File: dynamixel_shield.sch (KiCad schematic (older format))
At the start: 21 parts, among them P1 BARREL_JACK, P2 CONN_01X02, P3 CONN_01X03, P4 CONN_01X03, P5 CONN_01X03, P6 CONN_01X03, P7 CONN_01X03, P8 CONN_01X03, P9 CONN_01X03, Q1 MOSFET_N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

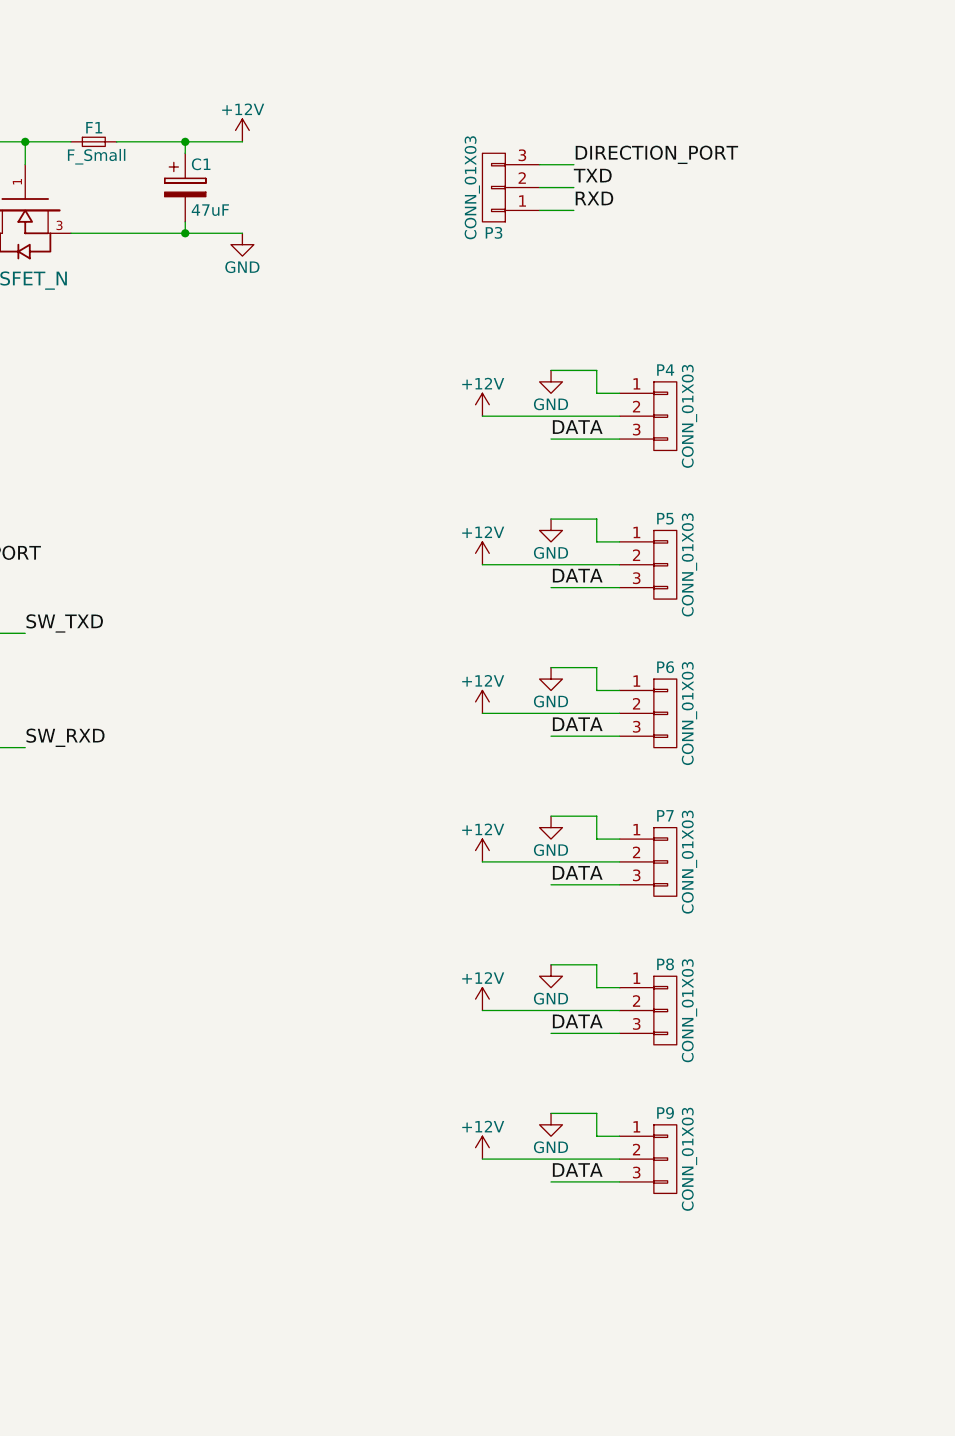
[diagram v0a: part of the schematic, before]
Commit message: Add power on LED
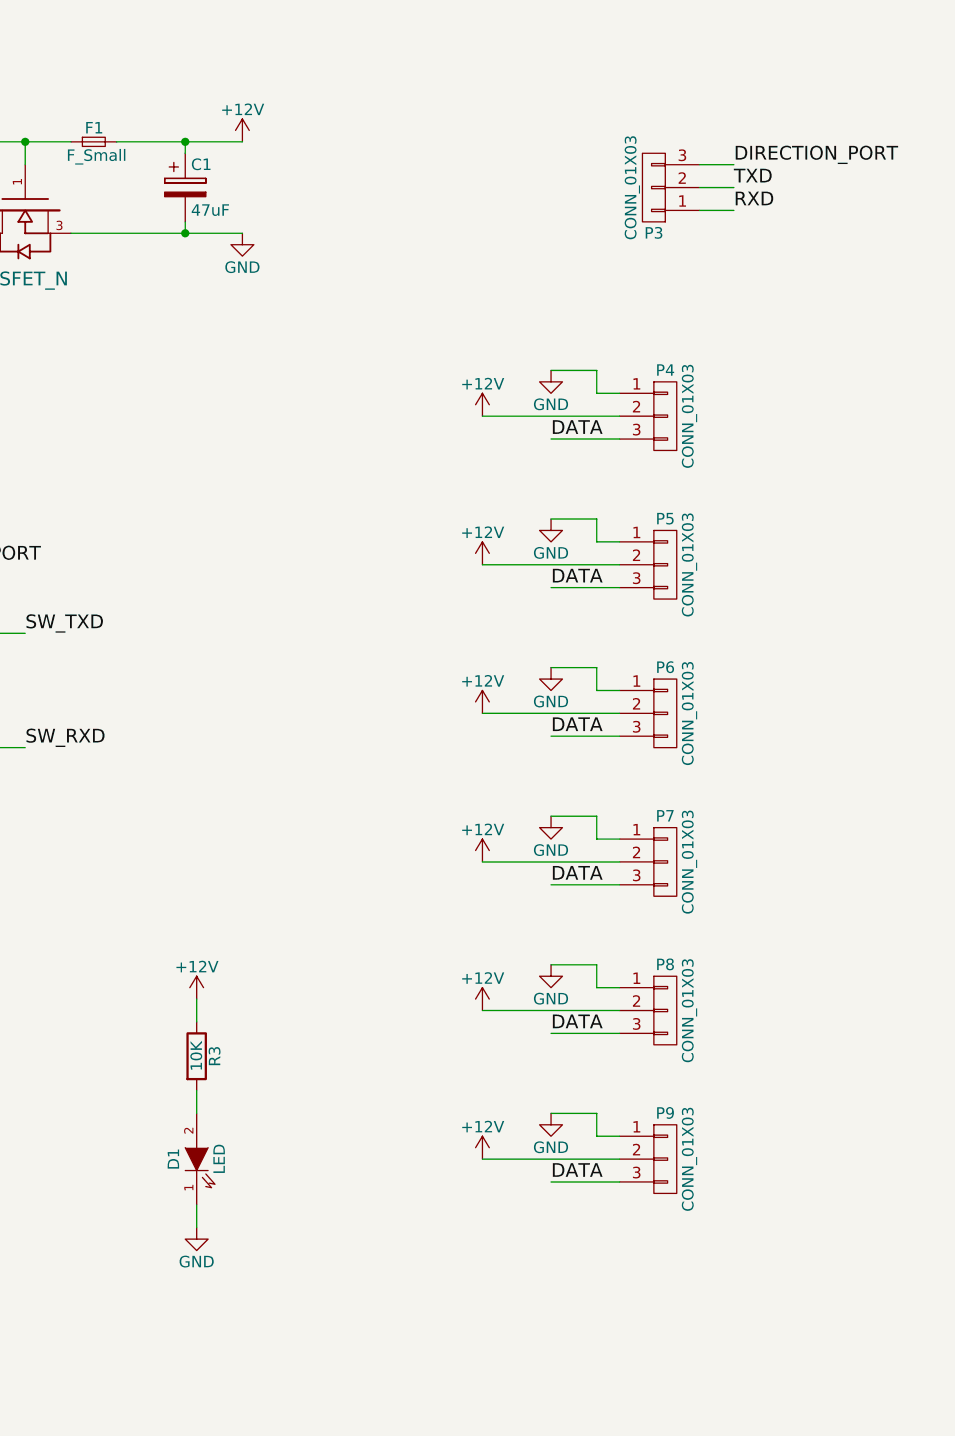
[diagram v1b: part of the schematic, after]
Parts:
- added D1: LED, LEDs:LED_0603, symbol LED
- added R3: 10K, Resistors_SMD:R_0603_HandSoldering, symbol R
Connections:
- net +12V: now also R3.1
- net GND: now also D1.1 (K)
- new net: D1.2 (A), R3.2
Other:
- moved on the sheet: P3
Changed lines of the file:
@@
 Text Label 3600 6650 0    60   ~ 0
 SW_RXD
-Text Label 9100 1550 0    60   ~ 0
+Text Label 9800 1550 0    60   ~ 0
 RXD
-Text Label 9100 1450 0    60   ~ 0
+Text Label 9800 1450 0    60   ~ 0
 TXD
-Text Label 9100 1350 0    60   ~ 0
+Text Label 9800 1350 0    60   ~ 0
 DIRECTION_PORT
 Text Label 6050 3100 0    60   ~ 0
@@
 L CONN_01X03 P3
 U 1 1 57B600E0
-P 8750 1450
-F 0 "P3" H 8750 1650 50  0000 C CNN
-F 1 "CONN_01X03" V 8850 1450 50  0000 C CNN
-F 2 "Pin_Headers:Pin_Header_Angled_1x03" H 8750 1450 50  0001 C CNN
-F 3 "" H 8750 1450 50  0000 C CNN
-	1    8750 1450
+P 9450 1450
+F 0 "P3" H 9450 1650 50  0000 C CNN
+F 1 "CONN_01X03" V 9550 1450 50  0000 C CNN
+F 2 "Pin_Headers:Pin_Header_Angled_1x03" H 9450 1450 50  0001 C CNN
+F 3 "" H 9450 1450 50  0000 C CNN
+	1    9450 1450
 	-1   0    0    1
 $EndComp
@@
 	3400 6650 3600 6650
 Wire Wire Line
-	8950 1350 9100 1350
-Wire Wire Line
-	9100 1450 8950 1450
-Wire Wire Line
-	8950 1550 9100 1550
+	9650 1350 9800 1350
+Wire Wire Line
+	9800 1450 9650 1450
+Wire Wire Line
+	9650 1550 9800 1550
 Wire Wire Line
 	4550 2850 5800 2850
@@
 Wire Wire Line
 	6000 1650 6100 1650
+$Comp
+L LED D1
+U 1 1 57BDD735
+P 7450 5700
+F 0 "D1" H 7450 5800 50  0000 C CNN
+F 1 "LED" H 7450 5600 50  0000 C CNN
+F 2 "LEDs:LED_0603" H 7450 5700 50  0001 C CNN
+F 3 "" H 7450 5700 50  0000 C CNN
+	1    7450 5700
+	0    -1   -1   0
+$EndComp
+$Comp
+L R R3
+U 1 1 57BDD91F
+P 7450 5250
+F 0 "R3" V 7530 5250 50  0000 C CNN
+F 1 "10K" V 7450 5250 50  0000 C CNN
+F 2 "Resistors_SMD:R_0603_HandSoldering" V 7380 5250 50  0001 C CNN
+F 3 "" H 7450 5250 50  0000 C CNN
+	1    7450 5250
+	1    0    0    -1
+$EndComp
+Wire Wire Line
+	7450 5400 7450 5500
+$Comp
+L +12V #PWR?
+U 1 1 57BDE386
+P 7450 5000
+F 0 "#PWR?" H 7450 4850 50  0001 C CNN
+F 1 "+12V" H 7450 5140 50  0000 C CNN
+F 2 "" H 7450 5000 50  0000 C CNN
+F 3 "" H 7450 5000 50  0000 C CNN
+	1    7450 5000
+	1    0    0    -1
+$EndComp
+$Comp
+L GND #PWR?
+U 1 1 57BDE3DF
+P 7450 6000
+F 0 "#PWR?" H 7450 5750 50  0001 C CNN
+F 1 "GND" H 7450 5850 50  0000 C CNN
+F 2 "" H 7450 6000 50  0000 C CNN
+F 3 "" H 7450 6000 50  0000 C CNN
+	1    7450 6000
+	1    0    0    -1
+$EndComp
+Wire Wire Line
+	7450 5000 7450 5100
+Wire Wire Line
+	7450 5900 7450 6000
 $EndSCHEMATC

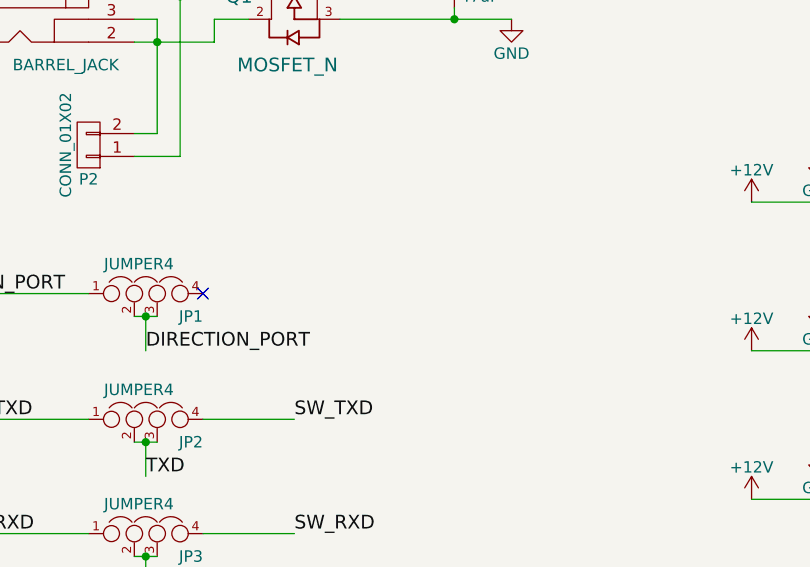
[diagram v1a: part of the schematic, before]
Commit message: Fix error in schematics
Arduino direction port was not connected in the SW configuration.
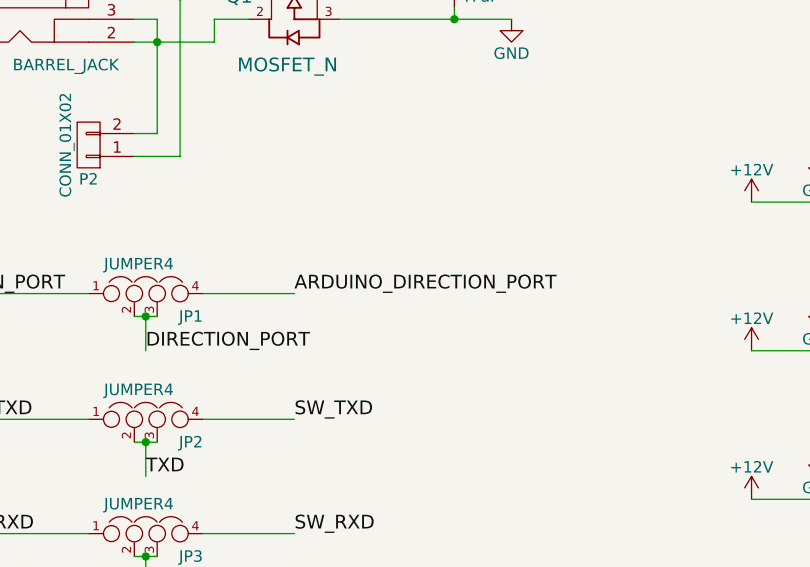
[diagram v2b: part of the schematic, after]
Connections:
- net ARDUINO_DIRECTION_PORT: now also JP1.4
- no-connect marks 26 -> 25
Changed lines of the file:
@@
 	1    0    0    -1
 $EndComp
-NoConn ~ 6300 2850
 Wire Wire Line
 	2100 5600 1900 5600
@@
 Wire Wire Line
 	7450 5900 7450 6000
+Text Label 6700 2850 0    60   ~ 0
+ARDUINO_DIRECTION_PORT
+Wire Wire Line
+	6300 2850 6700 2850
 $EndSCHEMATC

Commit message: move ext connector to make place for the fourth mounting hole
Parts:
- SHIELD1: footprint arduino:Arduino_shield -> arduino:Arduino_shield_dynamixel
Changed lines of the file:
@@
 F 0 "SHIELD1" H 2750 5250 60  0000 C CNN
 F 1 "ARDUINO_SHIELD" H 2750 7275 60  0000 C CNN
-F 2 "arduino:Arduino_shield" H 2950 7600 60  0001 C CNN
+F 2 "arduino:Arduino_shield_dynamixel" H 2950 7600 60  0001 C CNN
 F 3 "" H 2950 7600 60  0000 C CNN
 	1    2750 6150

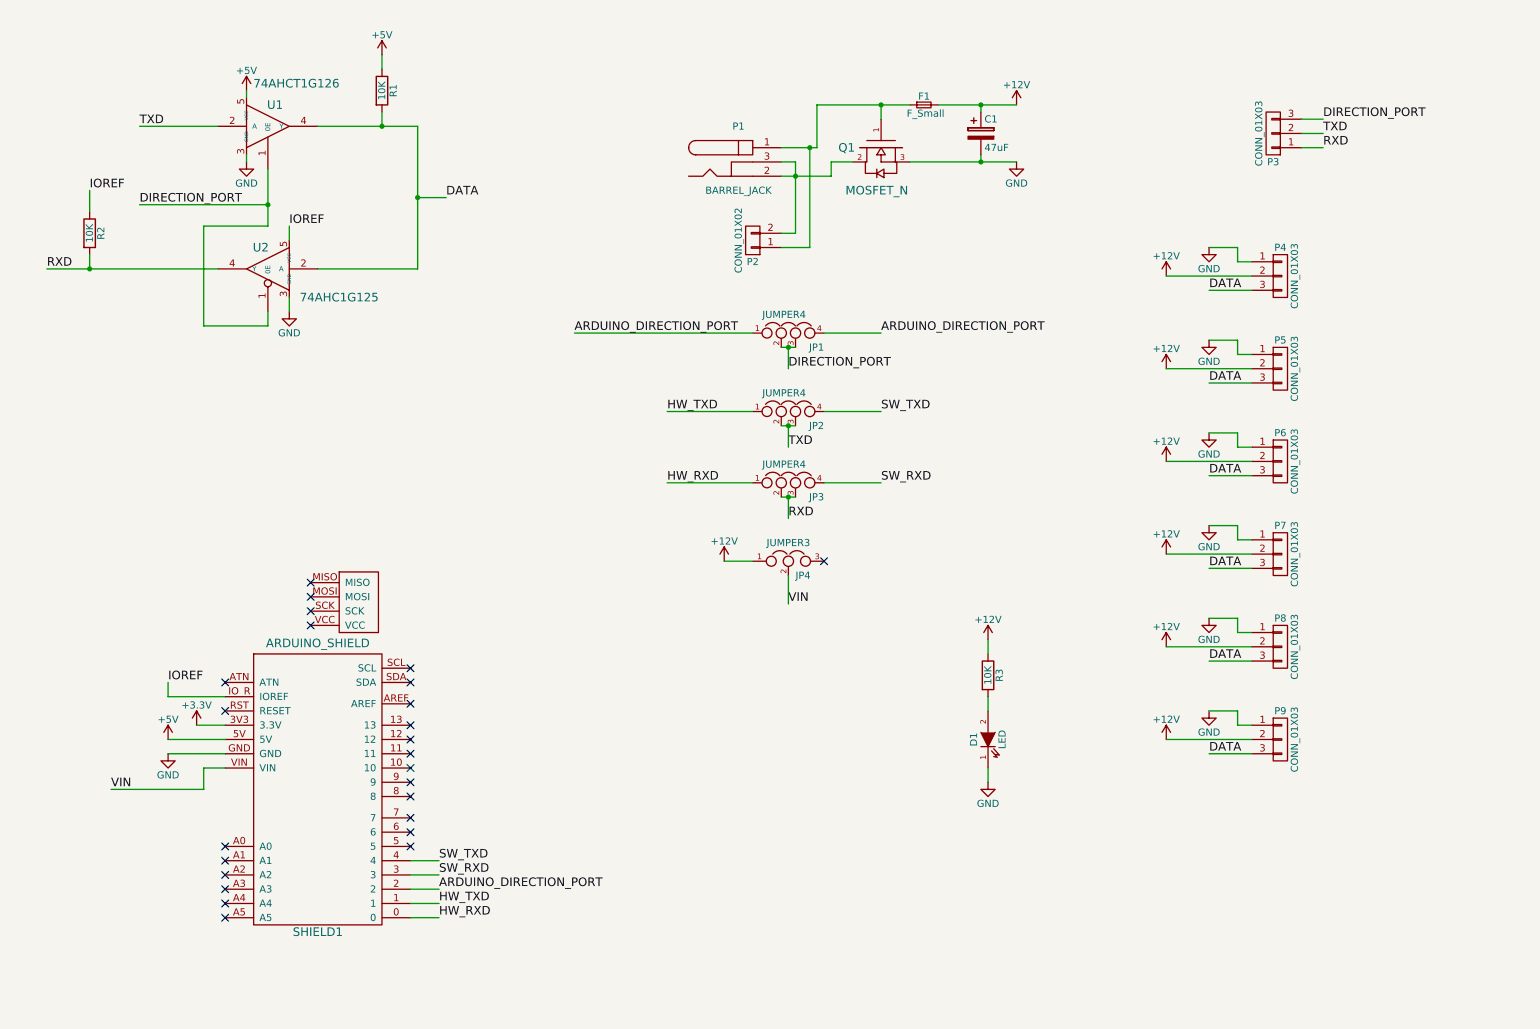
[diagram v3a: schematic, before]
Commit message: add annotation to the schematic
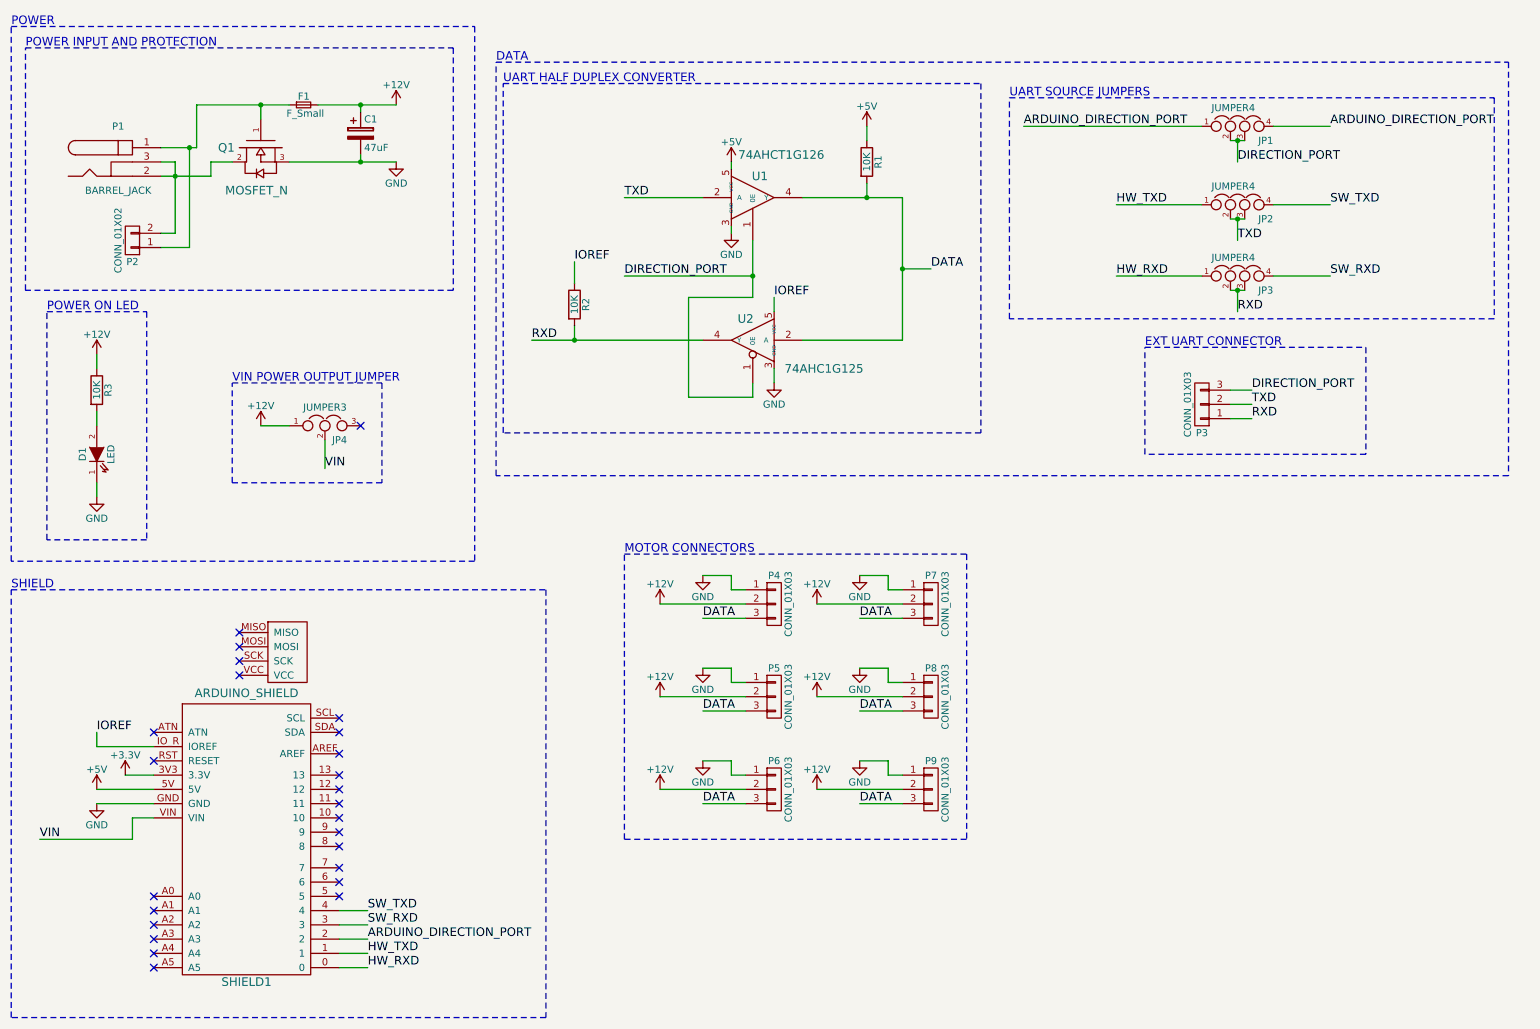
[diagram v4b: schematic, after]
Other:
- note added: "DATA"
- note added: "EXT UART CONNECTOR"
- note added: "MOTOR CONNECTORS"
- note added: "POWER"
- note added: "POWER INPUT AND PROTECTION"
- note added: "POWER ON LED"
- note added: "SHIELD"
- note added: "UART HALF DUPLEX CONVERTER"
- note added: "UART SOURCE JUMPERS"
- note added: "VIN POWER OUTPUT JUMPER"
- moved on the sheet: C1, D1, F1, JP1, JP2, JP3, JP4, P1, P2, P3, P4, P5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

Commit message: change capacitor height (bom related only, footprint is the same)
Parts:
- C1: footprint Capacitors_SMD:c_elec_6.3x5.3 -> Capacitors_SMD:c_elec_6.3x5.8
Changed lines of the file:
@@
 F 0 "C1" H 3075 1550 50  0000 L CNN
 F 1 "47uF" H 3075 1350 50  0000 L CNN
-F 2 "Capacitors_SMD:c_elec_6.3x5.3" H 3088 1300 50  0001 C CNN
+F 2 "Capacitors_SMD:c_elec_6.3x5.8" H 3088 1300 50  0001 C CNN
 F 3 "" H 3050 1450 50  0000 C CNN
 	1    3050 1450
@@
 	1200 3400 1200 3500
 $Comp
-L +12V #PWR?
+L +12V #PWR023
 U 1 1 57BDE386
 P 1200 3000
-F 0 "#PWR?" H 1200 2850 50  0001 C CNN
+F 0 "#PWR023" H 1200 2850 50  0001 C CNN
 F 1 "+12V" H 1200 3140 50  0000 C CNN
 F 2 "" H 1200 3000 50  0000 C CNN
@@
 $EndComp
 $Comp
-L GND #PWR?
+L GND #PWR024
 U 1 1 57BDE3DF
 P 1200 4000
-F 0 "#PWR?" H 1200 3750 50  0001 C CNN
+F 0 "#PWR024" H 1200 3750 50  0001 C CNN
 F 1 "GND" H 1200 3850 50  0000 C CNN
 F 2 "" H 1200 4000 50  0000 C CNN

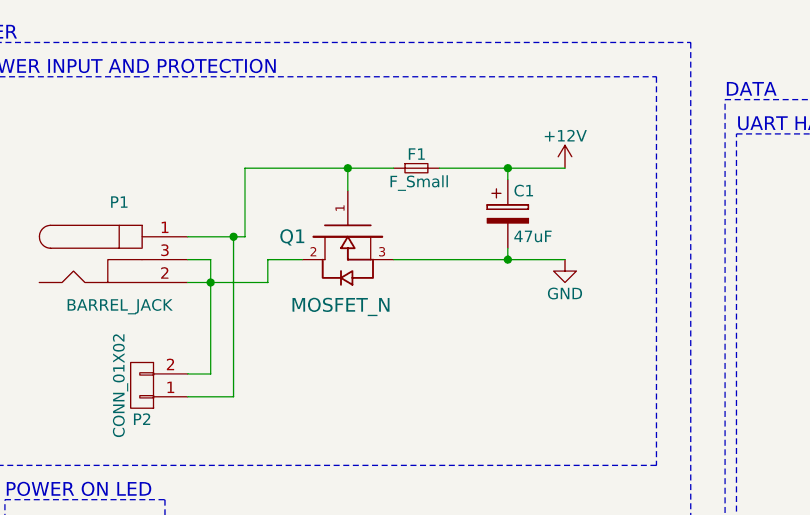
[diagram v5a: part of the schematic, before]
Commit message: put the fuse before the reverse voltage protection (thanks to bktemp from eevblog forum)
Quoting bktemp user on eevblog:

When the fuse fails, there will be a voltage spike.
Since there is no load except the mosfet gate, the voltage spike will damage the mosfet,
maybe even shorting gate-source and therefore the input supply.
If the gate is connected after the fuse, is will be connected in parallel with C1,
providing some protection for the sensitive gate.
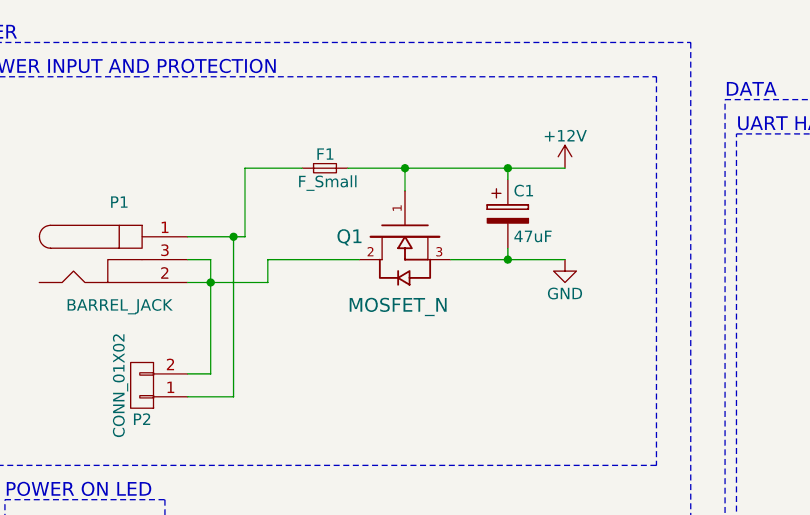
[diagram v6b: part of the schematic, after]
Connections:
- net +12V: now also Q1.1 (G)
- net at F1.1, P1.1, P2.1 (P1): no longer Q1.1 (G)
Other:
- moved on the sheet: F1, Q1
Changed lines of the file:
@@
 L MOSFET_N Q1
 U 1 1 57B22FDA
-P 2350 1550
-F 0 "Q1" V 2350 1850 60  0000 R CNN
-F 1 "MOSFET_N" V 2650 1800 60  0000 R CNN
-F 2 "TO_SOT_Packages_SMD:TO-252-2Lead" H 2350 1550 60  0001 C CNN
-F 3 "" H 2350 1550 60  0000 C CNN
-	1    2350 1550
+P 2600 1550
+F 0 "Q1" V 2600 1850 60  0000 R CNN
+F 1 "MOSFET_N" V 2900 1800 60  0000 R CNN
+F 2 "TO_SOT_Packages_SMD:TO-252-2Lead" H 2600 1550 60  0001 C CNN
+F 3 "" H 2600 1550 60  0000 C CNN
+	1    2600 1550
 	0    -1   1    0
 $EndComp
@@
 L F_Small F1
 U 1 1 57B5371B
-P 2650 1250
-F 0 "F1" H 2610 1310 50  0000 L CNN
-F 1 "F_Small" H 2530 1190 50  0000 L CNN
-F 2 "fuse:Fuseholder5x20_horiz_lateral" H 2650 1250 50  0001 C CNN
-F 3 "" H 2650 1250 50  0000 C CNN
-	1    2650 1250
+P 2250 1250
+F 0 "F1" H 2210 1310 50  0000 L CNN
+F 1 "F_Small" H 2130 1190 50  0000 L CNN
+F 2 "fuse:Fuseholder5x20_horiz_lateral" H 2250 1250 50  0001 C CNN
+F 3 "" H 2250 1250 50  0000 C CNN
+	1    2250 1250
 	1    0    0    -1
 $EndComp
@@
 	1900 1250 1900 1550
 Wire Wire Line
-	2350 1250 2350 1350
-Connection ~ 2350 1250
-Wire Wire Line
-	2550 1650 3300 1650
-Wire Wire Line
 	4900 1900 5450 1900
 Wire Wire Line
@@
 	2000 1750 2000 1650
 Wire Wire Line
-	2000 1650 2150 1650
-Wire Wire Line
-	1900 1250 2550 1250
-Wire Wire Line
-	2750 1250 3300 1250
+	2000 1650 2400 1650
+Wire Wire Line
+	2350 1250 3300 1250
 Wire Wire Line
 	1750 1650 1750 2150
@@
 Wire Notes Line
 	4000 3850 4000 950
+Wire Wire Line
+	3300 1650 2800 1650
+Wire Wire Line
+	2150 1250 1900 1250
+Wire Wire Line
+	2600 1350 2600 1250
+Connection ~ 2600 1250
 $EndSCHEMATC
